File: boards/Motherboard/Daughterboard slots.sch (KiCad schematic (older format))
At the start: 6 parts

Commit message: Annotated parts in dboard slots sheet
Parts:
- gave numbers to parts that had none: 6
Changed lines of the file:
@@
 LIBS:CONN_16
 LIBS:csmall
-LIBS:dboardheader-22
 LIBS:Motherboard-cache
 EELAYER 27 0
@@
 Sheet 7 7
 Title "Daughterboard interface"
-Date "25 jun 2014"
+Date "26 jun 2014"
 Rev ""
 Comp "TimVideos"
@@
 NoConn ~ 2950 2450
 $Comp
-L DIL20 P?
+L DIL20 P701
 U 1 1 53ABDD4A
 P 2600 2600
-F 0 "P?" H 2600 3150 70  0000 C CNN
+F 0 "P701" H 2600 3150 70  0000 C CNN
 F 1 "SLOT-A" V 2600 2600 70  0000 C CNN
 F 2 "" H 2600 2600 60  0000 C CNN
@@
 NoConn ~ 6100 2450
 $Comp
-L DIL20 P?
+L DIL20 P702
 U 1 1 53ABE4E4
 P 5750 2600
-F 0 "P?" H 5750 3150 70  0000 C CNN
+F 0 "P702" H 5750 3150 70  0000 C CNN
 F 1 "SLOT-B" V 5750 2600 70  0000 C CNN
 F 2 "" H 5750 2600 60  0000 C CNN
@@
 NoConn ~ 9100 2450
 $Comp
-L DIL20 P?
+L DIL20 P703
 U 1 1 53ABE51C
 P 8750 2600
-F 0 "P?" H 8750 3150 70  0000 C CNN
+F 0 "P703" H 8750 3150 70  0000 C CNN
 F 1 "SLOT-C" V 8750 2600 70  0000 C CNN
 F 2 "" H 8750 2600 60  0000 C CNN
@@
 NoConn ~ 2900 4350
 $Comp
-L DIL20 P?
+L DIL20 P704
 U 1 1 53ABE54F
 P 2550 4500
-F 0 "P?" H 2550 5050 70  0000 C CNN
+F 0 "P704" H 2550 5050 70  0000 C CNN
 F 1 "SLOT-D" V 2550 4500 70  0000 C CNN
 F 2 "" H 2550 4500 60  0000 C CNN
@@
 NoConn ~ 6050 4350
 $Comp
-L DIL20 P?
+L DIL20 P705
 U 1 1 53ABE579
 P 5700 4500
-F 0 "P?" H 5700 5050 70  0000 C CNN
+F 0 "P705" H 5700 5050 70  0000 C CNN
 F 1 "SLOT-E" V 5700 4500 70  0000 C CNN
 F 2 "" H 5700 4500 60  0000 C CNN
@@
 NoConn ~ 9050 4350
 $Comp
-L DIL20 P?
+L DIL20 P706
 U 1 1 53ABE5A3
 P 8700 4500
-F 0 "P?" H 8700 5050 70  0000 C CNN
+F 0 "P706" H 8700 5050 70  0000 C CNN
 F 1 "SLOT-F" V 8700 4500 70  0000 C CNN
 F 2 "" H 8700 4500 60  0000 C CNN

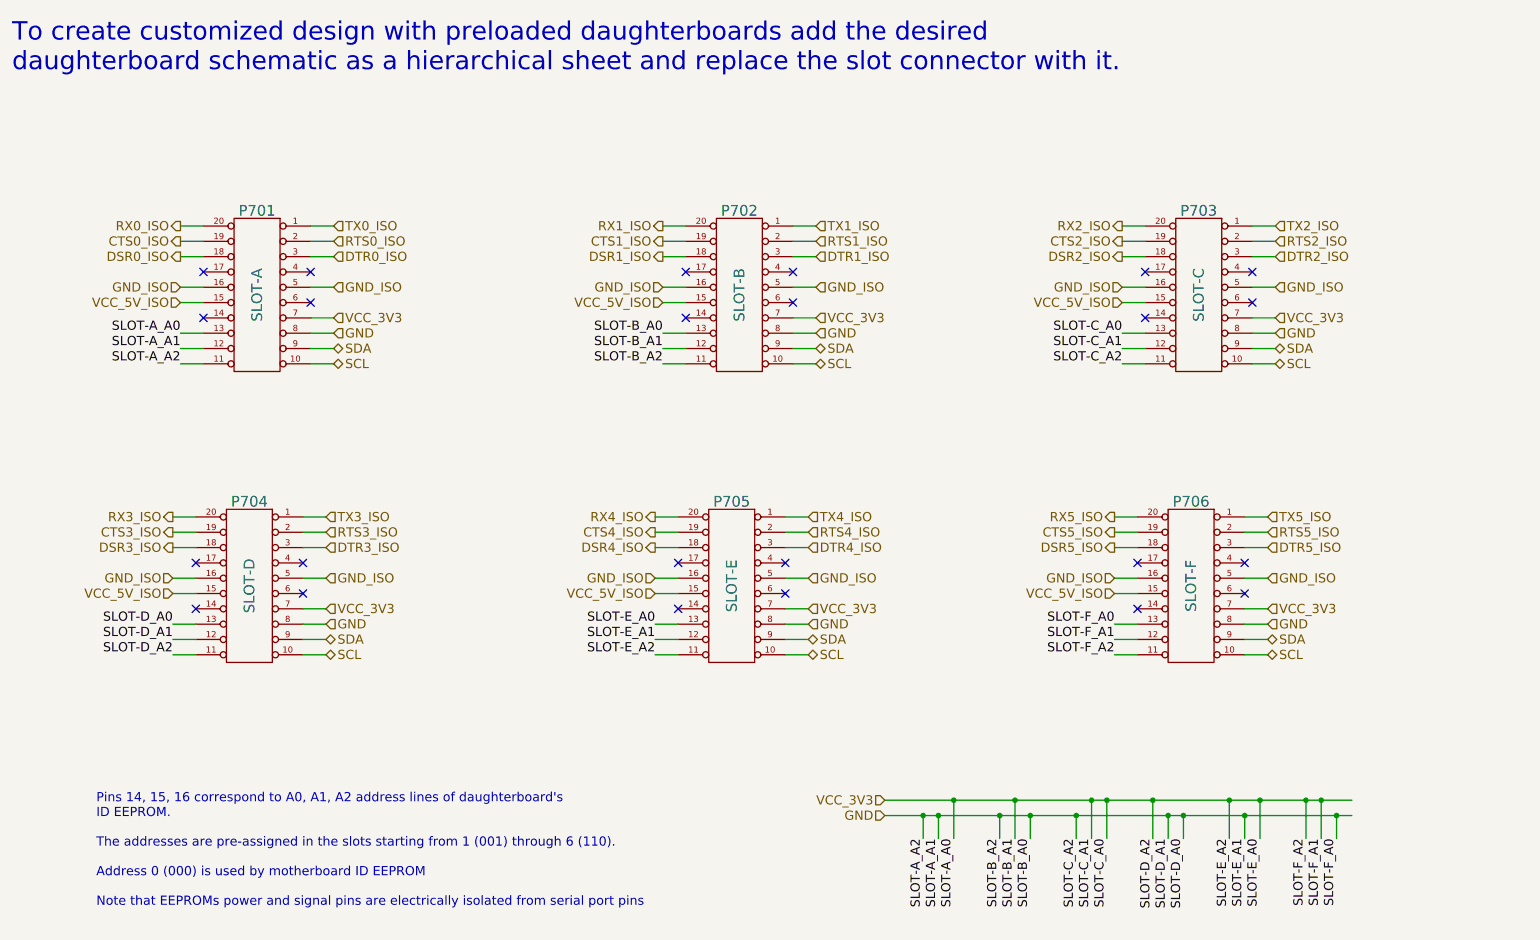
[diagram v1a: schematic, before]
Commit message: Change to 5 serial port; Connect Atlys and PIC18F SPI; Entire schematic updated
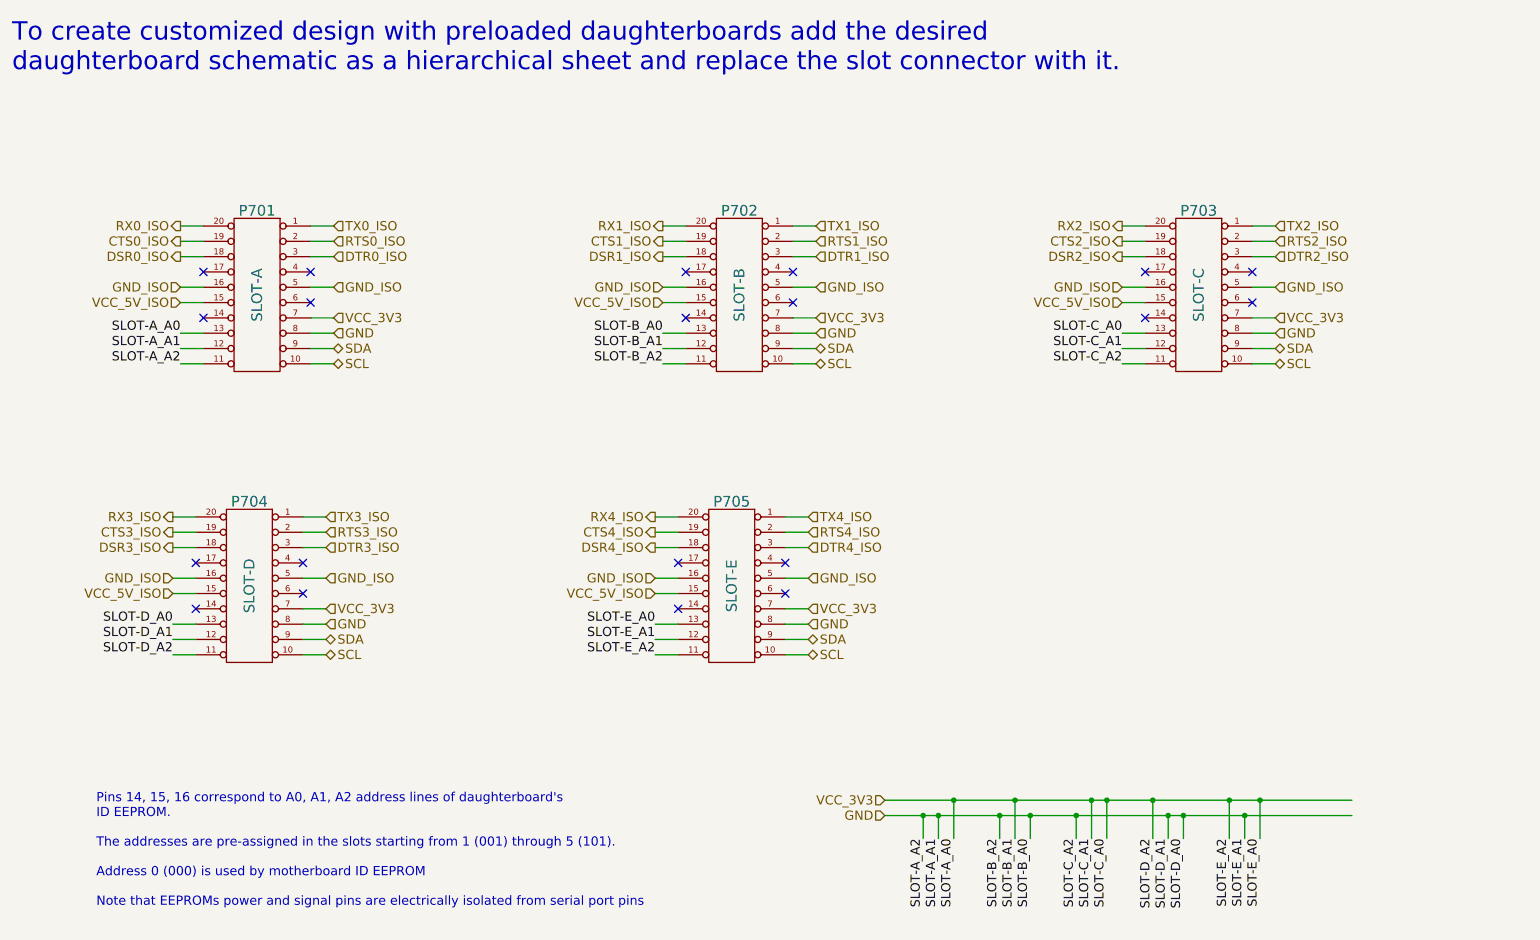
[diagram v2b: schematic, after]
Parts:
- removed P706: SLOT-F, symbol DIL20
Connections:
- no-connect marks 24 -> 20
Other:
- note added: "Pins 14, 15, 16 correspond to A0, A1, A2 address lines of daughterboard's \nID EEPROM. \n\nThe addresses are pre-assigned in the slots starting from 1 (001) through 5 (101).\n\nAddress 0 (000) is used by motherboard ID EEPROM\n\nNote that EEPROMs power and signal pins are electrically isolated from serial port pins"
- note removed: "Pins 14, 15, 16 correspond to A0, A1, A2 address lines of daughterboard's \nID EEPROM. \n\nThe addresses are pre-assigned in the slots starting from 1 (001) through 6 (110).\n\nAddress 0 (000) is used by motherboard ID EEPROM\n\nNote that EEPROMs power and signal pins are electrically isolated from serial port pins"
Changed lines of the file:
@@
 $Descr A4 11693 8268
 encoding utf-8
-Sheet 7 7
+Sheet 6 7
 Title "Daughterboard interface"
-Date "26 jun 2014"
+Date "30 jun 2014"
 Rev ""
 Comp "TimVideos"
@@
 GND
 Text Notes 1550 6600 0    60   ~ 0
-Pins 14, 15, 16 correspond to A0, A1, A2 address lines of daughterboard's \nID EEPROM. \n\nThe addresses are pre-assigned in the slots starting from 1 (001) through 6 (110).\n\nAddress 0 (000) is used by motherboard ID EEPROM\n\nNote that EEPROMs power and signal pins are electrically isolated from serial port pins
+Pins 14, 15, 16 correspond to A0, A1, A2 address lines of daughterboard's \nID EEPROM. \n\nThe addresses are pre-assigned in the slots starting from 1 (001) through 5 (101).\n\nAddress 0 (000) is used by motherboard ID EEPROM\n\nNote that EEPROMs power and signal pins are electrically isolated from serial port pins
 Text Label 2100 2850 2    60   ~ 0
 SLOT-A_A0
@@
 Text HLabel 6700 6000 0    60   Input ~ 0
 GND
-Text Label 9650 6150 3    60   ~ 0
-SLOT-F_A0
-Text Label 9550 6150 3    60   ~ 0
-SLOT-F_A1
-Text Label 9450 6150 3    60   ~ 0
-SLOT-F_A2
 Text HLabel 2100 2550 0    60   Input ~ 0
 GND_ISO
@@
 NoConn ~ 5350 4650
 NoConn ~ 6050 4550
-Text HLabel 8200 4050 0    60   Output ~ 0
-RX5_ISO
-Text HLabel 9200 4050 2    60   Input ~ 0
-TX5_ISO
-Text HLabel 9200 4150 2    60   Input ~ 0
-RTS5_ISO
-Text HLabel 8200 4150 0    60   Output ~ 0
-CTS5_ISO
-Text HLabel 9200 4250 2    60   Input ~ 0
-DTR5_ISO
-Text HLabel 8200 4250 0    60   Output ~ 0
-DSR5_ISO
-Text HLabel 8200 4550 0    60   Input ~ 0
-VCC_5V_ISO
-Text HLabel 9200 4450 2    60   Input ~ 0
-GND_ISO
-Text HLabel 9200 4850 2    60   BiDi ~ 0
-SDA
-Text HLabel 9200 4950 2    60   BiDi ~ 0
-SCL
-Text HLabel 9200 4650 2    60   Input ~ 0
-VCC_3V3
-Text HLabel 9200 4750 2    60   Input ~ 0
-GND
-Text Label 8200 4750 2    60   ~ 0
-SLOT-F_A0
-Text Label 8200 4850 2    60   ~ 0
-SLOT-F_A1
-Text Label 8200 4950 2    60   ~ 0
-SLOT-F_A2
-Text HLabel 8200 4450 0    60   Input ~ 0
-GND_ISO
-NoConn ~ 8350 4350
-NoConn ~ 9050 4350
-$Comp
-L DIL20 P706
-U 1 1 53ABE5A3
-P 8700 4500
-F 0 "P706" H 8700 5050 70  0000 C CNN
-F 1 "SLOT-F" V 8700 4500 70  0000 C CNN
-F 2 "" H 8700 4500 60  0000 C CNN
-F 3 "" H 8700 4500 60  0000 C CNN
-	1    8700 4500
-	-1   0    0    -1
-$EndComp
-NoConn ~ 8350 4650
-NoConn ~ 9050 4550
 Text Label 9150 6150 3    60   ~ 0
 SLOT-E_A0
@@
 	6700 6000 9750 6000
 Wire Wire Line
-	9550 5900 9550 6150
-Wire Wire Line
-	9450 5900 9450 6150
-Wire Wire Line
 	2100 2550 2250 2550
 Wire Wire Line
@@
 Wire Wire Line
 	5200 4450 5350 4450
-Wire Wire Line
-	9050 4050 9200 4050
-Wire Wire Line
-	8350 4050 8200 4050
-Wire Wire Line
-	9050 4150 9200 4150
-Wire Wire Line
-	8350 4150 8200 4150
-Wire Wire Line
-	9050 4250 9200 4250
-Wire Wire Line
-	8350 4250 8200 4250
-Wire Wire Line
-	8200 4550 8350 4550
-Wire Wire Line
-	9200 4450 9050 4450
-Wire Wire Line
-	9200 4850 9050 4850
-Wire Wire Line
-	9200 4950 9050 4950
-Wire Wire Line
-	9200 4750 9050 4750
-Wire Wire Line
-	9200 4650 9050 4650
-Wire Wire Line
-	8200 4750 8350 4750
-Wire Wire Line
-	8350 4850 8200 4850
-Wire Wire Line
-	8200 4950 8350 4950
-Wire Wire Line
-	8200 4450 8350 4450
-Wire Wire Line
-	9650 6000 9650 6150
 Wire Wire Line
 	9050 6000 9050 6150
@@
 Connection ~ 9050 6000
 Connection ~ 9150 5900
-Connection ~ 9450 5900
-Connection ~ 9550 5900
-Connection ~ 9650 6000
 $EndSCHEMATC

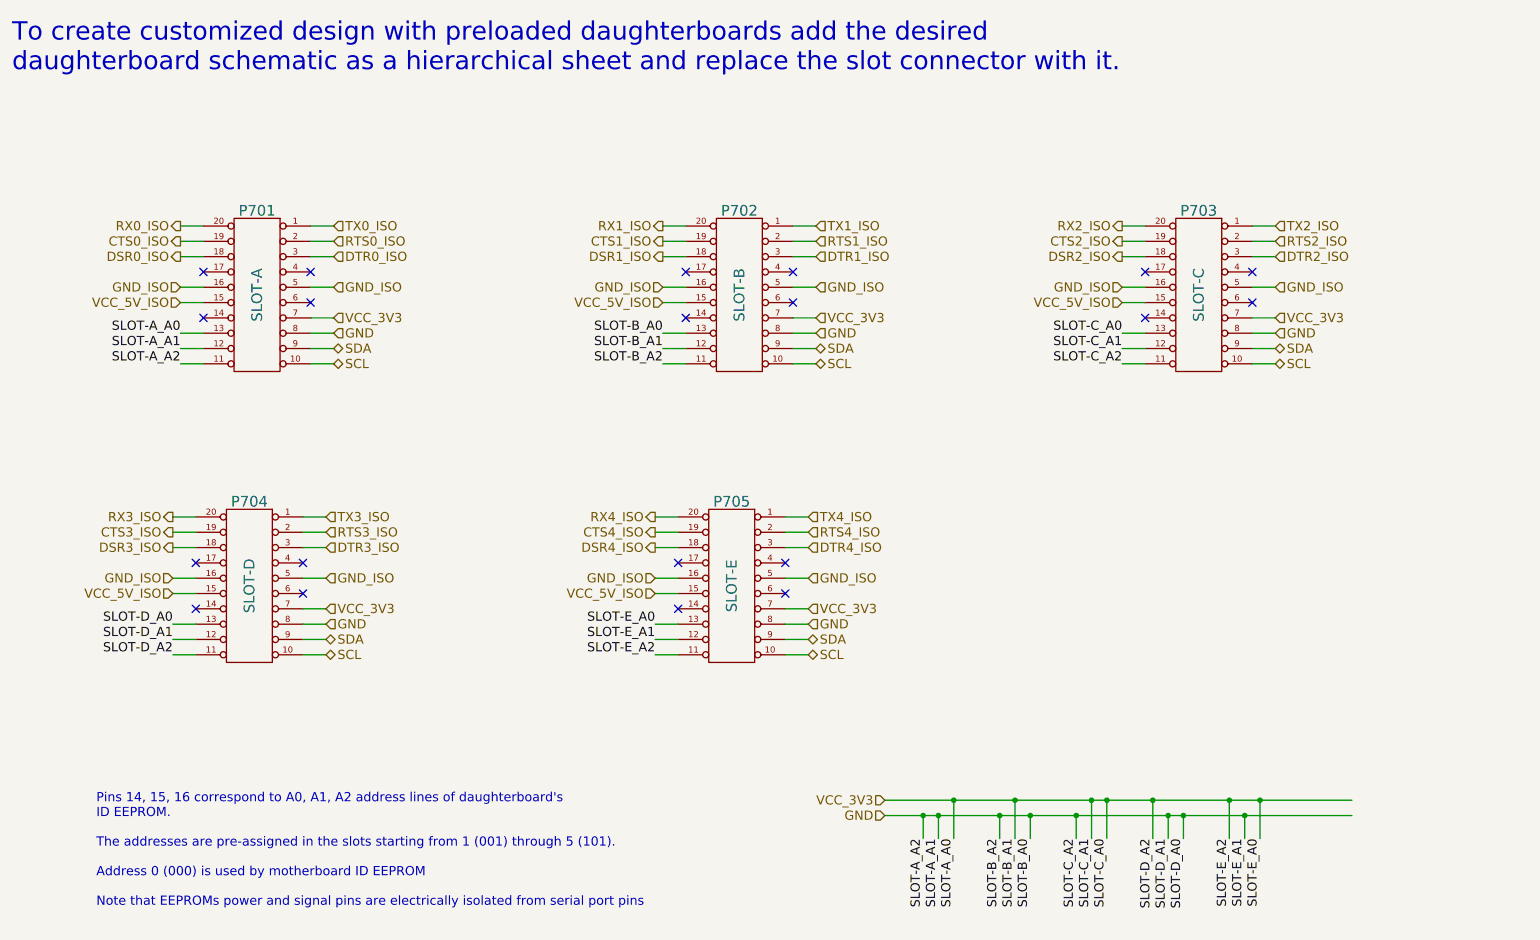
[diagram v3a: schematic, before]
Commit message: Updated daughterboard header pinout in all sheets to be PMOD UART 4/4A compatible
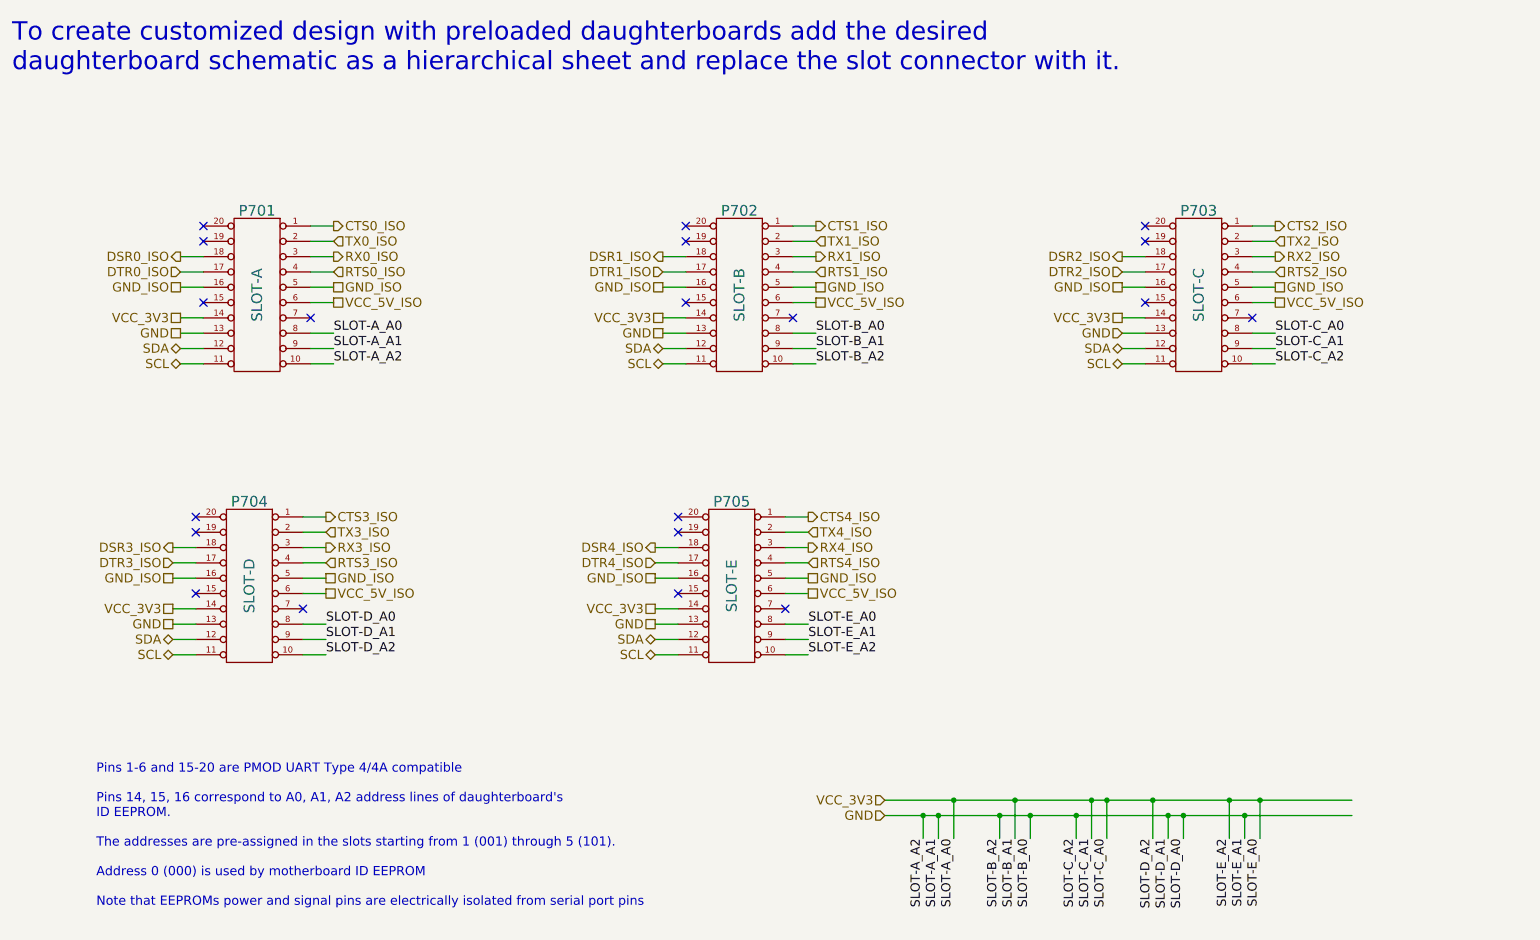
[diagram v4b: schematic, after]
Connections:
- net CTS0_ISO: now also P701.1 (P1); no longer P701.19 (P19)
- net CTS1_ISO: now also P702.1 (P1); no longer P702.19 (P19)
- net CTS2_ISO: now also P703.1 (P1); no longer P703.19 (P19)
- net CTS3_ISO: now also P704.1 (P1); no longer P704.19 (P19)
- net CTS4_ISO: now also P705.1 (P1); no longer P705.19 (P19)
- net DTR0_ISO: now also P701.17 (P17); no longer P701.3 (P3)
- net DTR1_ISO: now also P702.17 (P17); no longer P702.3 (P3)
- net DTR2_ISO: now also P703.17 (P17); no longer P703.3 (P3)
- net DTR3_ISO: now also P704.17 (P17); no longer P704.3 (P3)
- net DTR4_ISO: now also P705.17 (P17); no longer P705.3 (P3)
- net GND: now also P701.10 (P10), P701.13 (P13), P701.9 (P9), P702.10 (P10), P703.10 (P10), P703.13 (P13), P704.9 (P9), P705.13 (P13), P705.9 (P9); no longer P701.11 (P11), P701.12 (P12), P701.8 (P8), P702.11 (P11), P703.11 (P11), P703.8 (P8), P704.12 (P12), P705.12 (P12), P705.8 (P8)
- net RTS0_ISO: now also P701.4 (P4); no longer P701.2 (P2)
- net RTS1_ISO: now also P702.4 (P4); no longer P702.2 (P2)
- net RTS2_ISO: now also P703.4 (P4); no longer P703.2 (P2)
- net RTS3_ISO: now also P704.4 (P4); no longer P704.2 (P2)
- net RTS4_ISO: now also P705.4 (P4); no longer P705.2 (P2)
- net RX0_ISO: now also P701.3 (P3); no longer P701.20 (P20)
- net RX1_ISO: now also P702.3 (P3); no longer P702.20 (P20)
- net RX2_ISO: now also P703.3 (P3); no longer P703.20 (P20)
- net RX3_ISO: now also P704.3 (P3); no longer P704.20 (P20)
- net RX4_ISO: now also P705.3 (P3); no longer P705.20 (P20)
- net SCL: now also P701.11 (P11), P702.11 (P11), P703.11 (P11), P704.11 (P11), P705.11 (P11); no longer P701.10 (P10), P702.10 (P10), P703.10 (P10), P704.10 (P10), P705.10 (P10)
- net SDA: now also P701.12 (P12), P702.12 (P12), P703.12 (P12), P704.12 (P12), P705.12 (P12); no longer P701.9 (P9), P702.9 (P9), P703.9 (P9), P704.9 (P9), P705.9 (P9)
- net TX0_ISO: now also P701.2 (P2); no longer P701.1 (P1)
- net TX1_ISO: now also P702.2 (P2); no longer P702.1 (P1)
- net TX2_ISO: now also P703.2 (P2); no longer P703.1 (P1)
- net TX3_ISO: now also P704.2 (P2); no longer P704.1 (P1)
- net TX4_ISO: now also P705.2 (P2); no longer P705.1 (P1)
- net VCC_3V3: now also P701.14 (P14), P701.8 (P8), P702.14 (P14), P702.9 (P9), P703.14 (P14), P703.8 (P8), P703.9 (P9), P704.10 (P10), P704.14 (P14), P705.10 (P10), P705.14 (P14), P705.8 (P8); no longer P701.13 (P13), P701.7 (P7), P702.12 (P12), P702.7 (P7), P703.12 (P12), P703.13 (P13), P703.7 (P7), P704.11 (P11), P704.7 (P7), P705.11 (P11), P705.13 (P13), P705.7 (P7)
- net VCC_5V_ISO: now also P701.6 (P6), P702.6 (P6), P703.6 (P6), P704.6 (P6), P705.6 (P6); no longer P701.15 (P15), P702.15 (P15), P703.15 (P15), P704.15 (P15), P705.15 (P15)
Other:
- note added: "Pins 1-6 and 15-20 are PMOD UART Type 4/4A compatible\n\nPins 14, 15, 16 correspond to A0, A1, A2 address lines of daughterboard's \nID EEPROM. \n\nThe addresses are pre-assigned in the slots starting from 1 (001) through 5 (101).\n\nAddress 0 (000) is used by motherboard ID EEPROM\n\nNote that EEPROMs power and signal pins are electrically isolated from serial port pins"
- note removed: "Pins 14, 15, 16 correspond to A0, A1, A2 address lines of daughterboard's \nID EEPROM. \n\nThe addresses are pre-assigned in the slots starting from 1 (001) through 5 (101).\n\nAddress 0 (000) is used by motherboard ID EEPROM\n\nNote that EEPROMs power and signal pins are electrically isolated from serial port pins"
